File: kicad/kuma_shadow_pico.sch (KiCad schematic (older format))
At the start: 9 parts

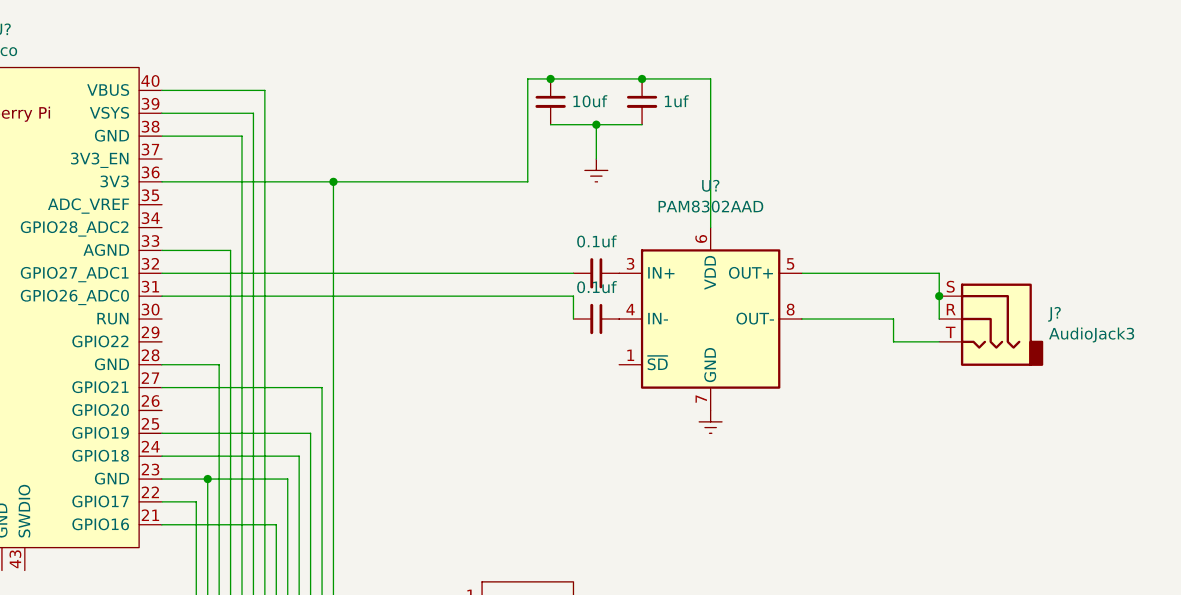
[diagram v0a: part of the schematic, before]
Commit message: took it back to keyboard input only
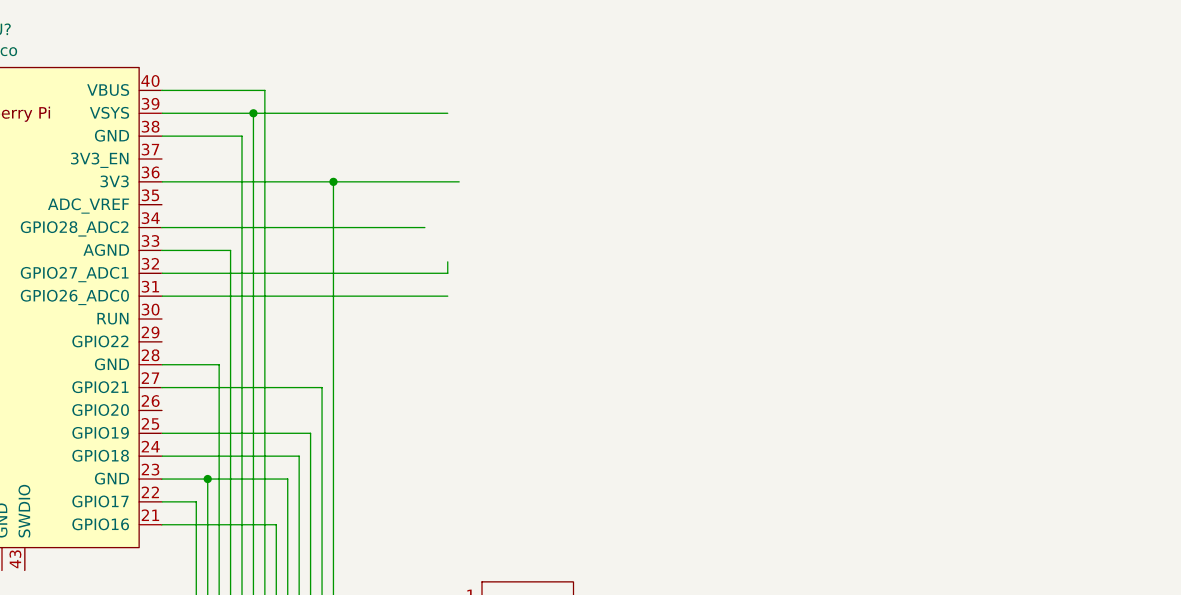
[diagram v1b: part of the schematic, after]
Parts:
- removed Capacitor1, Capacitor2: 0.1uf, symbol Device:C_Small
- removed Capacitor3: 10uf, symbol Device:C_Small
- removed Capacitor4: 1uf, symbol Device:C_Small
- removed J?: AudioJack3, symbol Connector:AudioJack3
- removed U?: PAM8302AAD, symbol Amplifier_Audio:PAM8302AAD
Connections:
- net labels removed: GNDREF
- wire segments 93 -> 81
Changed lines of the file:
@@
 EESchema Schematic File Version 4
+LIBS:kuma_shadow_pico-cache
 EELAYER 30 0
 EELAYER END
@@
 $EndComp
 $Comp
-L Amplifier_Audio:PAM8302AAD U?
-U 1 1 60EA77EB
-P 8850 3050
-F 0 "U?" H 8850 3631 50  0000 C CNN
-F 1 "PAM8302AAD" H 8850 3540 50  0000 C CNN
-F 2 "" H 8850 3050 50  0001 C CNN
-F 3 "https://www.diodes.com/assets/Datasheets/PAM8302A.pdf" H 8850 3050 50  0001 C CNN
-	1    8850 3050
-	1    0    0    -1
-$EndComp
-$Comp
-L Device:C_Small Capacitor1
-U 1 1 60EA83B1
-P 8350 3050
-F 0 "Capacitor1" V 8121 3050 50  0001 C CNN
-F 1 "0.1uf" V 8213 3050 50  0000 C CNN
-F 2 "" H 8350 3050 50  0001 C CNN
-F 3 "~" H 8350 3050 50  0001 C CNN
-	1    8350 3050
-	0    1    1    0
-$EndComp
-$Comp
-L Device:C_Small Capacitor2
-U 1 1 60EA86C2
-P 8350 2850
-F 0 "Capacitor2" V 8121 2850 50  0001 C CNN
-F 1 "0.1uf" V 8213 2850 50  0000 C CNN
-F 2 "" H 8350 2850 50  0001 C CNN
-F 3 "~" H 8350 2850 50  0001 C CNN
-	1    8350 2850
-	0    1    1    0
-$EndComp
-$Comp
-L Device:C_Small Capacitor3
-U 1 1 60EA892B
-P 8150 2100
-F 0 "Capacitor3" H 8242 2146 50  0001 L CNN
-F 1 "10uf" H 8242 2100 50  0000 L CNN
-F 2 "" H 8150 2100 50  0001 C CNN
-F 3 "~" H 8150 2100 50  0001 C CNN
-	1    8150 2100
-	1    0    0    -1
-$EndComp
-$Comp
-L Device:C_Small Capacitor4
-U 1 1 60EA8D78
-P 8550 2100
-F 0 "Capacitor4" H 8642 2146 50  0001 L CNN
-F 1 "1uf" H 8642 2100 50  0000 L CNN
-F 2 "" H 8550 2100 50  0001 C CNN
-F 3 "~" H 8550 2100 50  0001 C CNN
-	1    8550 2100
-	1    0    0    -1
-$EndComp
-$Comp
-L power:GNDREF #PWR?
-U 1 1 60EA971A
-P 8350 2350
-F 0 "#PWR?" H 8350 2100 50  0001 C CNN
-F 1 "GNDREF" H 8355 2177 50  0001 C CNN
-F 2 "" H 8350 2350 50  0001 C CNN
-F 3 "" H 8350 2350 50  0001 C CNN
-	1    8350 2350
-	1    0    0    -1
-$EndComp
-$Comp
-L power:GNDREF #PWR?
-U 1 1 60EA985B
-P 8850 3450
-F 0 "#PWR?" H 8850 3200 50  0001 C CNN
-F 1 "GNDREF" H 8855 3277 50  0001 C CNN
-F 2 "" H 8850 3450 50  0001 C CNN
-F 3 "" H 8850 3450 50  0001 C CNN
-	1    8850 3450
-	1    0    0    -1
-$EndComp
-$Comp
-L Connector:AudioJack3 J?
-U 1 1 60EA9F9F
-P 10050 3050
-F 0 "J?" H 9770 3075 50  0000 R CNN
-F 1 "AudioJack3" H 9770 2984 50  0000 R CNN
-F 2 "" H 10050 3050 50  0001 C CNN
-F 3 "~" H 10050 3050 50  0001 C CNN
-	1    10050 3050
-	-1   0    0    -1
-$EndComp
-Wire Wire Line
-	8150 2200 8350 2200
-Wire Wire Line
-	8350 2350 8350 2200
-Connection ~ 8350 2200
-Wire Wire Line
-	8350 2200 8550 2200
-Wire Wire Line
-	8550 2000 8850 2000
-Wire Wire Line
-	8850 2000 8850 2650
-Wire Wire Line
-	8550 2000 8150 2000
-Connection ~ 8550 2000
-Wire Wire Line
-	9250 2850 9850 2850
-Wire Wire Line
-	9850 2850 9850 2950
-Wire Wire Line
-	9250 3050 9650 3050
-Wire Wire Line
-	9650 3050 9650 3150
-Wire Wire Line
-	9650 3150 9850 3150
-Wire Wire Line
-	9850 3050 9850 2950
-Connection ~ 9850 2950
-$Comp
 L personal_symbol:Adafruit_MicroSD_Breakout U?
 U 1 1 60EBD894
@@
 $EndComp
 Wire Wire Line
-	8050 2000 8150 2000
-Connection ~ 8150 2000
-Wire Wire Line
-	8050 2450 7200 2450
-Wire Wire Line
-	8250 3050 8250 2950
-Wire Wire Line
-	8250 2950 6450 2950
-Wire Wire Line
-	6450 2850 8250 2850
-Wire Wire Line
 	6450 3850 6600 3850
 Wire Wire Line
@@
 	6850 5100 6850 2150
 Wire Wire Line
-	6850 2150 6450 2150
-Wire Wire Line
 	6500 4950 6900 4950
 Wire Wire Line
@@
 Wire Wire Line
 	6900 2050 6450 2050
-Wire Wire Line
-	8050 2000 8050 2450
 Wire Wire Line
 	5000 6900 4900 6900
@@
 Wire Wire Line
 	7200 4900 7200 2450
+Wire Wire Line
+	6450 2150 6850 2150
+Connection ~ 6850 2150
+Wire Wire Line
+	6850 2150 7700 2150
+Wire Wire Line
+	6450 2450 7200 2450
 Connection ~ 7200 2450
 Wire Wire Line
-	7200 2450 6450 2450
+	7200 2450 7750 2450
+Wire Wire Line
+	6450 2650 7600 2650
+Wire Wire Line
+	6450 2850 7700 2850
+Wire Wire Line
+	7700 2850 7700 2800
+Wire Wire Line
+	6450 2950 7700 2950
 $EndSCHEMATC
